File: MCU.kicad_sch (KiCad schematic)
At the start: 51 parts, among them J1 Conn_01x02_Pin, J2 Conn_01x02_Pin, SW1 XRSn_button, U5 F280025PNS, Y2 H130B-16.000-18-3030-EXT-TR

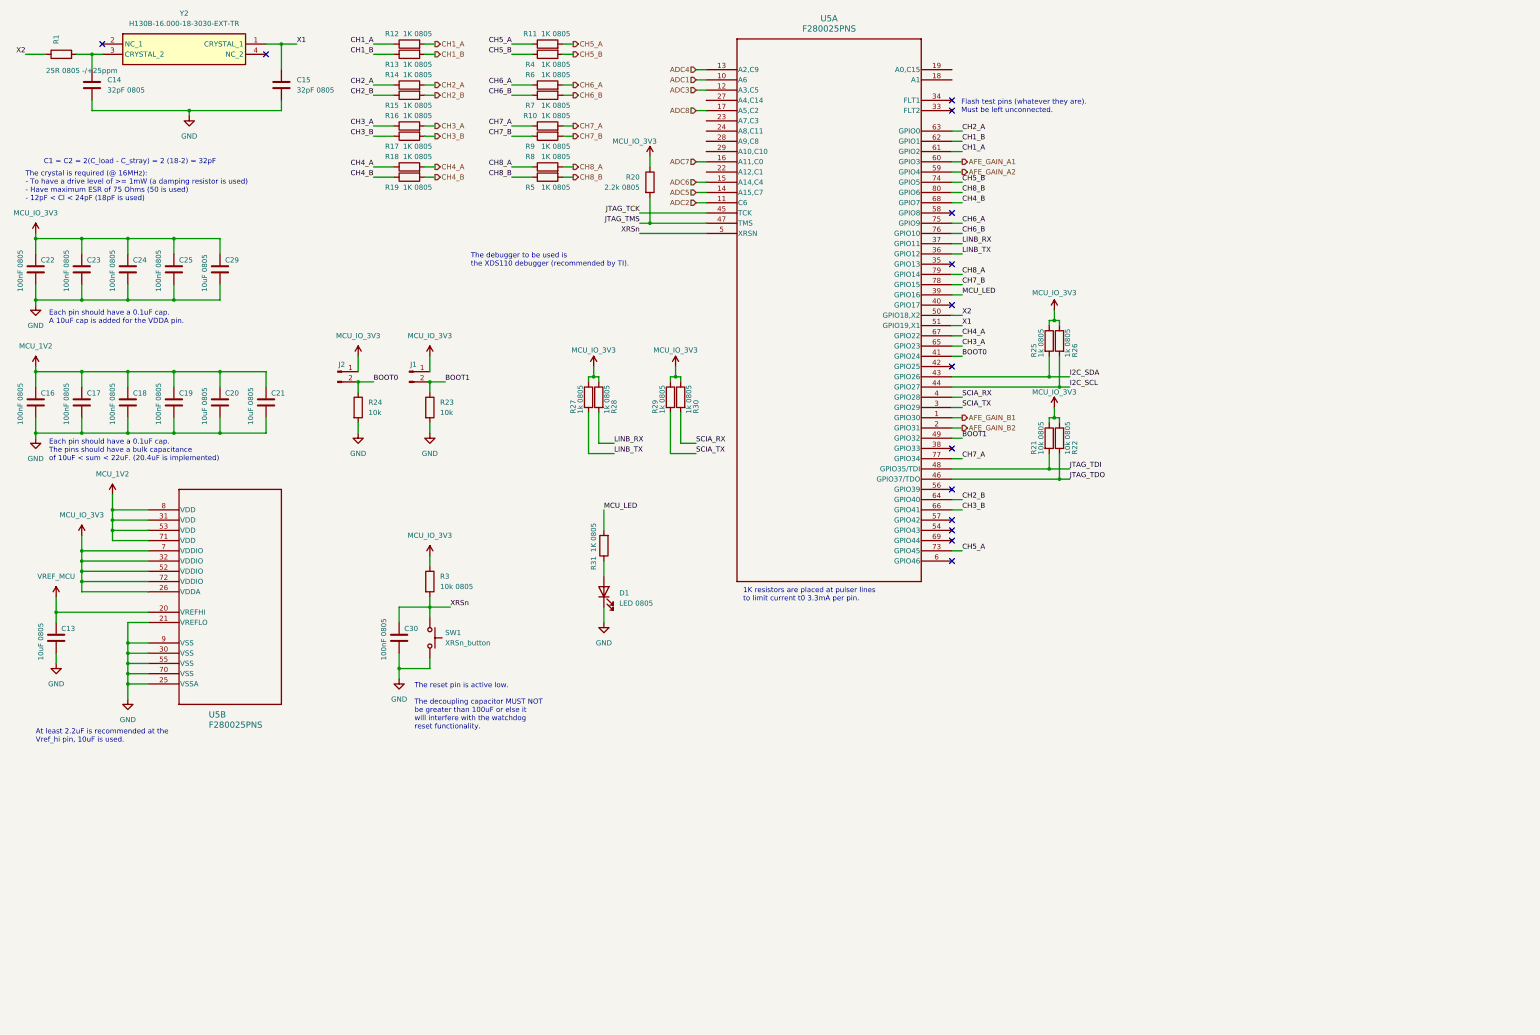
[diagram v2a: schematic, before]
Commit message: finished analog signal chain, added main power components, complete the schematic and form a power budget table
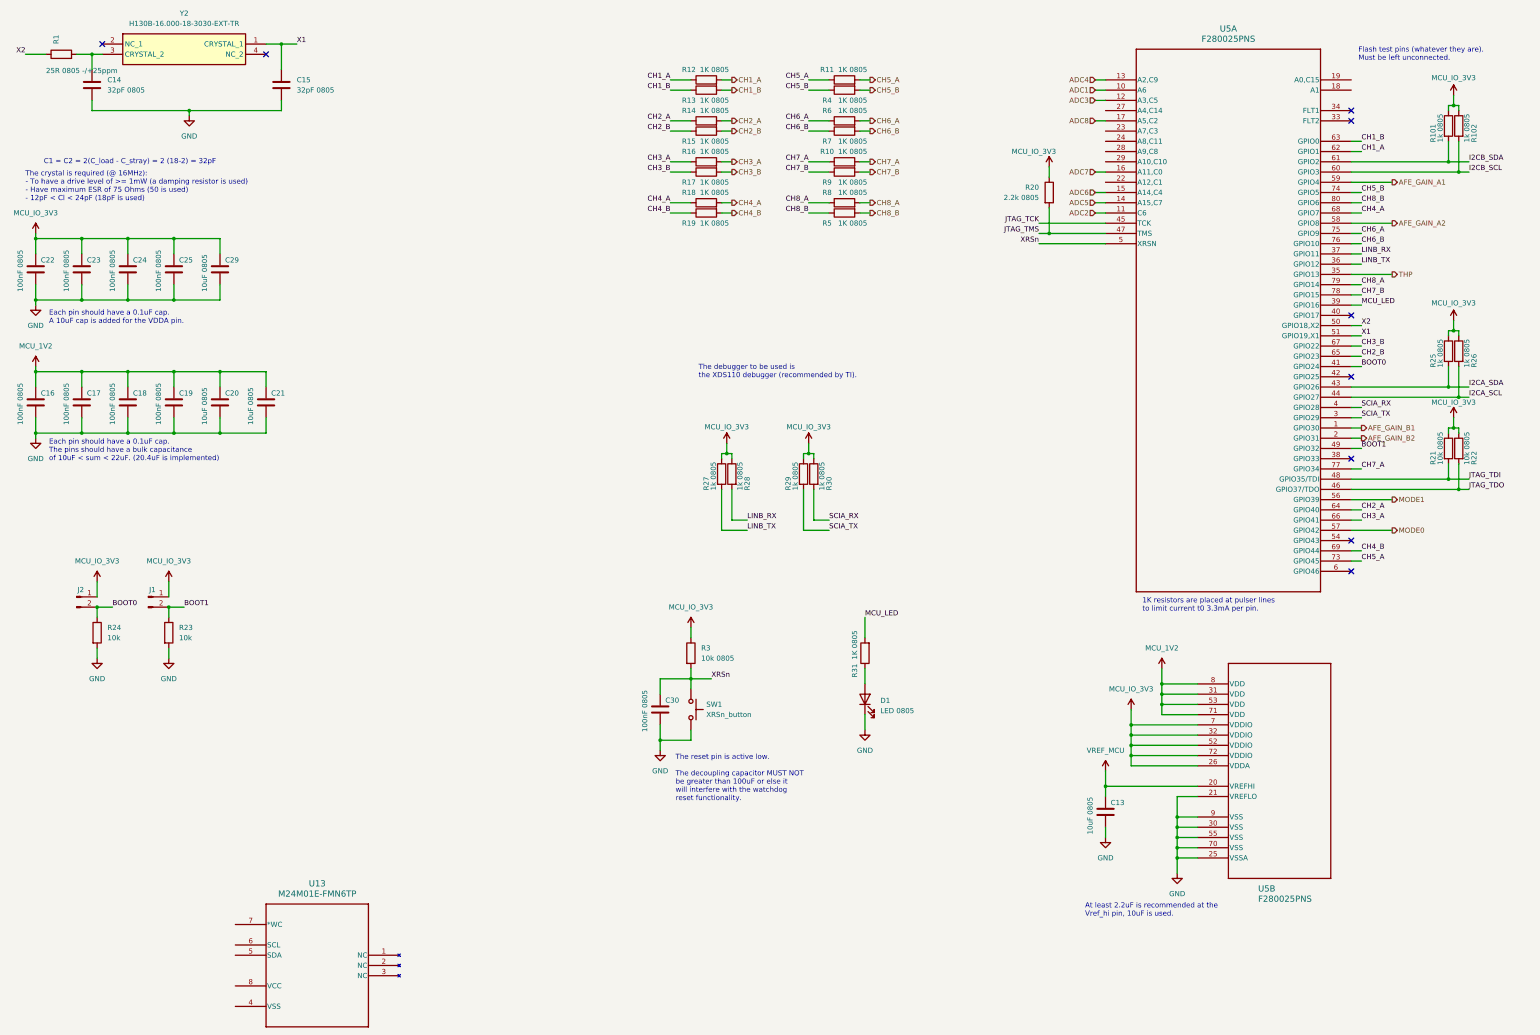
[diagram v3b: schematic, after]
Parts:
- added R101, R102: 1k 0805, symbol Device:R
- added U13: M24M01E-FMN6TP, SO8N_4X5X1P27_STM, symbol M24M01E-FMN6TP:M24M01E-FMN6TP
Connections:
- net AFE_GAIN_A1: now also U5.59 (GPIO4); no longer U5.60 (GPIO3)
- net AFE_GAIN_A2: now also U5.58 (GPIO8); no longer U5.59 (GPIO4)
- net CH1_A: now also U5.62 (GPIO1); no longer U5.61 (GPIO2)
- net CH1_B: now also U5.63 (GPIO0); no longer U5.62 (GPIO1)
- net CH2_A: now also U5.64 (GPIO40); no longer U5.63 (GPIO0)
- net CH2_B: now also U5.65 (GPIO23); no longer U5.64 (GPIO40)
- net CH3_A: now also U5.66 (GPIO41); no longer U5.65 (GPIO23)
- net CH3_B: now also U5.67 (GPIO22); no longer U5.66 (GPIO41)
- net CH4_A: now also U5.68 (GPIO7); no longer U5.67 (GPIO22)
- net CH4_B: now also U5.69 (GPIO44); no longer U5.68 (GPIO7)
- net MCU_IO_3V3: now also R101.1, R102.1
- net THP: now reaches U5.35 (GPIO13)
- net MODE1: now reaches U5.56 (GPIO39)
- net MODE0: now reaches U5.57 (GPIO42)
- net I2C_SCL renamed I2CA_SCL
- net I2C_SDA renamed I2CA_SDA
- new net I2CB_SCL: R102.2, U5.60 (GPIO3)
- new net I2CB_SDA: R101.2, U5.61 (GPIO2)
- no-connect marks 14 -> 9
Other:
- moved on the sheet: C13, C30, D1, J1, J2, R10, R11, R12, R13, R14, R15, R16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

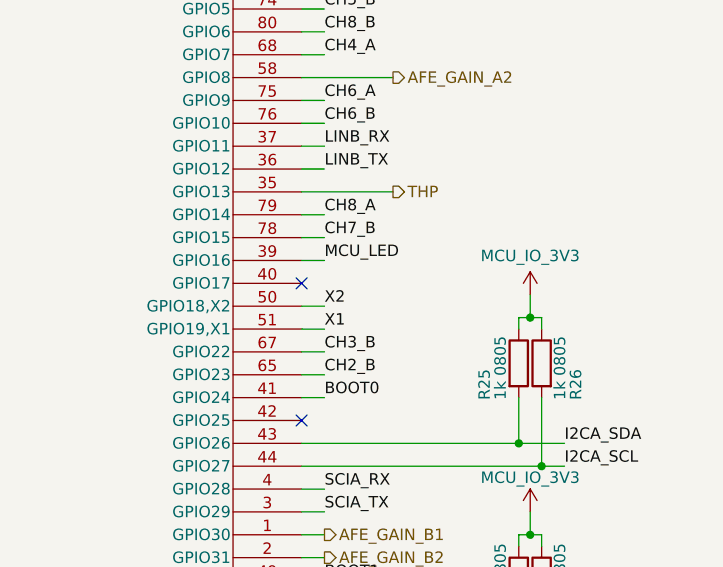
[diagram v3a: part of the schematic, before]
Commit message: finished 50% of power section, 50% remaining + EEPROM & revision
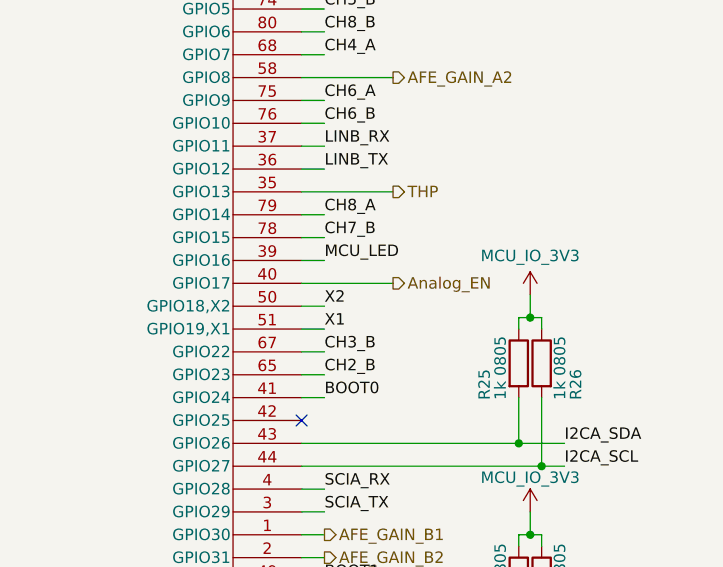
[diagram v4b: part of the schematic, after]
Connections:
- net Analog_EN: now reaches U5.40 (GPIO17)
- no-connect marks 9 -> 8
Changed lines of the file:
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@@
 	)
 	(no_connect
-		(at 345.44 88.9)
-	)
-	(no_connect
 		(at 345.44 104.14)
 	)
@@
 	(wire
 		(pts
+			(xy 345.44 88.9) (xy 355.6 88.9)
+		)
+		(stroke
+			(width 0)
+			(type default)
+		)
+	)
+	(wire
+		(pts
 			(xy 267.97 71.12) (xy 284.48 71.12)
 		)
@@
 		)
 	)
+	(hierarchical_label "Analog_EN"
+		(shape output)
+		(at 355.6 88.9 0)
+		(effects
+			(font
+				(size 1.27 1.27)
+			)
+			(justify left)
+		)
+	)

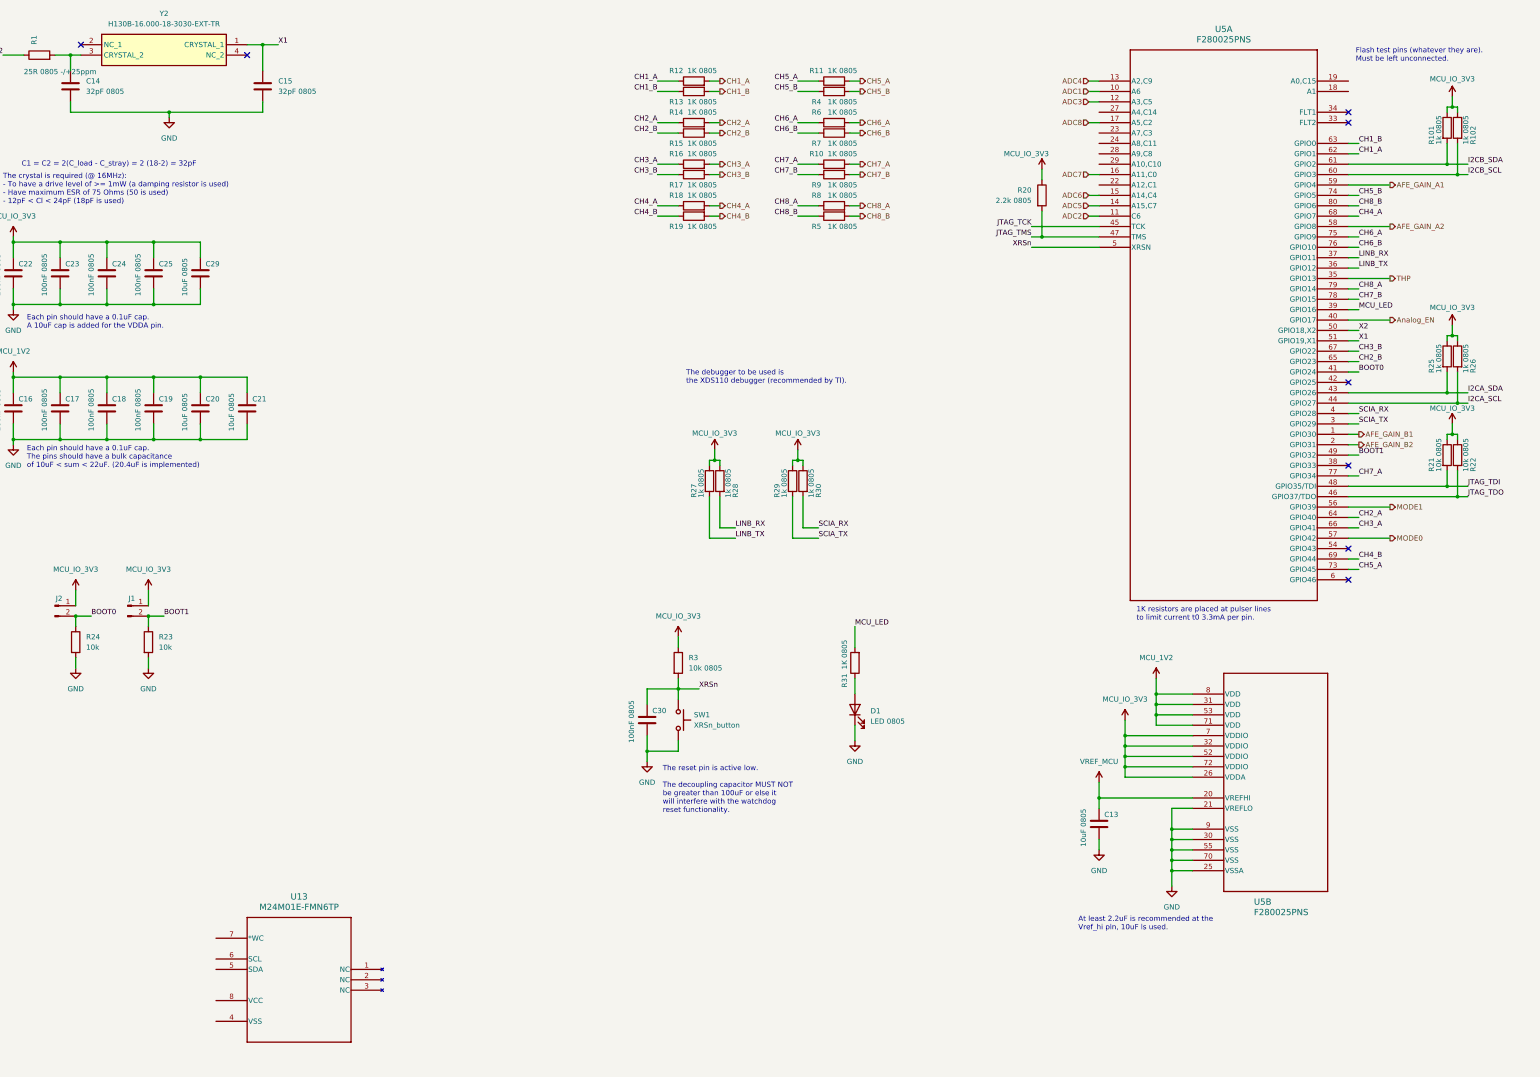
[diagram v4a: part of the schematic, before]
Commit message: 95% done, only headers for communication & power are remaining + RS232 transceiver & 1.5v reference
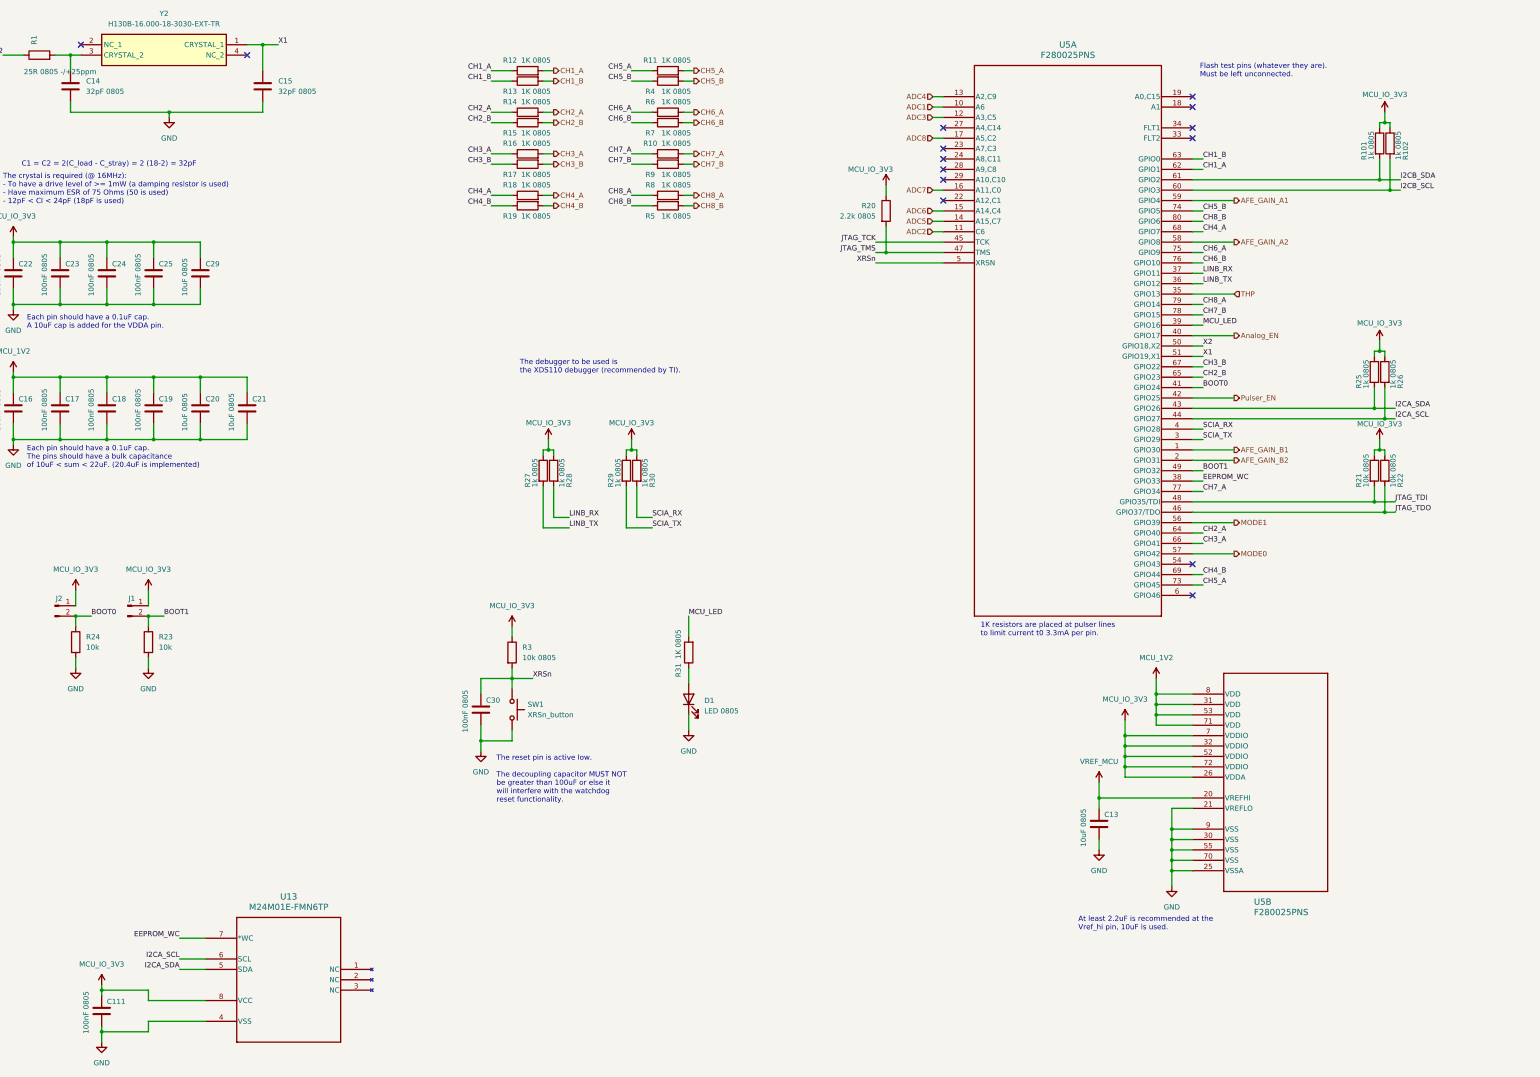
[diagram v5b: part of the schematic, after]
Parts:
- added C111: 100nF 0805, symbol Device:C
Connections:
- net GND: now also U13.4 (VSS), C111.2
- net I2CA_SCL: now also U13.6 (SCL)
- net I2CA_SDA: now also U13.5 (SDA)
- net MCU_IO_3V3: now also U13.8 (VCC), C111.1
- net EEPROM_WC: now reaches U5.38 (GPIO33)
- net EEPROM_WC: now also U13.7 (*WC)
- net Pulser_EN: now reaches U5.42 (GPIO25)
- no-connect marks 8 -> 14
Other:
- moved on the sheet: C30, D1, R10, R101, R102, R11, R12, R13, R14, R15, R16, R17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

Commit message: DONE (inshallah)
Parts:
- added C112, C113, C114, C115, C116, C117: 100nF, symbol Device:C
- added J11: Logger Connector, symbol Connector:Conn_01x03_Pin
- added J12: UART Connector, symbol Connector:Conn_01x03_Pin
- added J13: External UART, digikey-footprints:PinHeader_1x3_P2.5mm_Drill1.1mm, symbol dk_Rectangular-Connectors-Headers-Male-Pins:B3B-XH-A_LF__SN_
- added J14: External I2C, digikey-footprints:PinHeader_1x3_P2.5mm_Drill1.1mm, symbol dk_Rectangular-Connectors-Headers-Male-Pins:B3B-XH-A_LF__SN_
- added J15: JTAG Header, symbol Connector:Conn_01x07_Pin
- added JP19, JP20, JP21: SolderJumper_2_Open, symbol Jumper:SolderJumper_2_Open
- added TP61, TP62, TP63, TP64, TP65, TP66, TP67, TP68, TP69, TP70, TP71, TP72: RCT-0C, digikey-footprints:PROBE_PAD_0805, symbol dk_Test-Points:RCT-0C
- added U17: TRS3221EIPWR, TRS3221EIPWR:SOP65P640X120-16N, symbol TRS3221EIPWR:TRS3221EIPWR
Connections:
- net BOOT0: now also JP19.1 (A)
- net BOOT1: now also JP20.1 (A)
- net CH1_A: now also TP62.1
- net CH1_B: now also TP61.1
- net GND: now also C114.2, C115.2, C116.2, C117.2, J11.3 (Pin_3), J12.3 (Pin_3), J13.1, J14.1, J15.7 (Pin_7), U17.1 (~{EN}), U17.14 (GND)
- net I2CA_SCL: now also TP64.1
- net I2CA_SDA: now also TP63.1
- net I2CB_SCL: now also J14.2, TP68.1
- net I2CB_SDA: now also J14.3, TP67.1
- net JTAG_TCK: now also J15.5 (Pin_5)
- net JTAG_TDI: now also J15.3 (Pin_3), TP65.1
- net JTAG_TDO: now also J15.4 (Pin_4), TP66.1
- net JTAG_TMS: now also J15.6 (Pin_6)
- net LINB_RX: now also J12.1 (Pin_1), TP69.1, U17.9 (ROUT)
- net LINB_TX: now also J12.2 (Pin_2), TP70.1, U17.11 (DIN)
- net MCU_IO_3V3: now also C116.1, C117.1, J15.1 (Pin_1), JP19.2 (B), JP20.2 (B), U17.15 (VCC)
- net SCIA_RX: now also J13.3, TP71.1
- net SCIA_TX: now also J13.2, TP72.1
- net XRSn: now also JP21.2 (B)
- net RS232_FOFF: now reaches U5.54 (GPIO43)
- net RS232_FOFF: now also U17.16 (~{FORCEOFF})
- net RS232_FON: now reaches U5.6 (GPIO46)
- net RS232_FON: now also U17.12 (FORCEON)
- new net: C112.1, U17.2 (C1+)
- new net: C112.2, U17.4 (C1-)
- new net: C115.1, U17.3 (V+)
- new net: C113.1, U17.5 (C2+)
- new net: C113.2, U17.6 (C2-)
- new net: C114.1, U17.7 (V-)
- new net: J15.2 (Pin_2), JP21.1 (A)
- new net RS232_RX: J11.1 (Pin_1), U17.8 (RIN)
- new net RS232_TX: J11.2 (Pin_2), U17.13 (DOUT)
- no-connect marks 14 -> 16
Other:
- note added: "The MCU has no dedicated JTAG reset pin (TRSTn) but theoretically this could work."
- moved on the sheet: C111, C13, C30, D1, J2, R23, R24, R27, R28, R29, R3, R30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

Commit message: started layout, 20-30% done
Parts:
- added J27: Conn_01x02_Pin, Connector_PinHeader_2.54mm:PinHeader_1x02_P2.54mm_Vertical, symbol Connector:Conn_01x02_Pin
- C111, C112, C113, C114, C115, C116, C117, C13, C14, C15, C16, C17, C18, C19, C20, C21, C22, C23, C24, C25, C29, C30: footprint (none) -> Capacitor_SMD:C_0603_1608Metric
- D1: footprint (none) -> LED_SMD:LED_0805_2012Metric
- J1, J2: footprint (none) -> Connector_PinHeader_2.54mm:PinHeader_1x02_P2.54mm_Vertical
- J11, J12: footprint (none) -> Connector_PinHeader_2.54mm:PinHeader_1x03_P2.54mm_Vertical
- J15: footprint (none) -> Connector_PinHeader_2.54mm:PinHeader_1x07_P2.54mm_Vertical
- JP19, JP20, JP21: footprint (none) -> Jumper:SolderJumper-2_P1.3mm_Open_Pad1.0x1.5mm
- R1, R10, R101, R102, R11, R12, R13, R14, R15, R16, R17, R18, R19, R20, R21, R22, R23, R24, R25, R26, R27, R28, R29, R3, R30, R31, R4, R5, R6, R7, R8, R9: footprint (none) -> Resistor_SMD:R_0603_1608Metric
- SW1: footprint (none) -> Button_Switch_SMD:SW_Push_SPST_NO_Alps_SKRK
- U13: footprint SO8N_4X5X1P27_STM -> M24M01E-FMN6TP:SO8N_4X5X1P27_STM
- U5: footprint PQFP_025PNSR_TEX -> F280025PNS:PQFP_025PNSR_TEX
- Y2: footprint H130B16000183030EXTTR -> KiCad:H130B16000183030EXTTR
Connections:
- net CH1_A: now also U5.80 (GPIO6); no longer TP62.1, U5.62 (GPIO1)
- net CH1_B: now also U5.79 (GPIO14); no longer TP61.1, U5.63 (GPIO0)
- net CH2_A: now also U5.78 (GPIO15); no longer U5.64 (GPIO40)
- net CH2_B: now also U5.77 (GPIO34); no longer U5.65 (GPIO23)
- net CH3_A: now also U5.76 (GPIO10); no longer U5.66 (GPIO41)
- net CH3_B: now also U5.75 (GPIO9); no longer U5.67 (GPIO22)
- net CH4_A: now also U5.74 (GPIO5); no longer U5.68 (GPIO7)
- net CH4_B: now also U5.73 (GPIO45); no longer U5.69 (GPIO44)
- net CH5_A: now also TP62.1, U5.62 (GPIO1); no longer U5.73 (GPIO45)
- net CH5_B: now also TP61.1, U5.63 (GPIO0); no longer U5.74 (GPIO5)
- net CH6_A: now also U5.64 (GPIO40); no longer U5.75 (GPIO9)
- net CH6_B: now also U5.65 (GPIO23); no longer U5.76 (GPIO10)
- net CH7_A: now also U5.66 (GPIO41); no longer U5.77 (GPIO34)
- net CH7_B: now also U5.67 (GPIO22); no longer U5.78 (GPIO15)
- net CH8_A: now also U5.68 (GPIO7); no longer U5.79 (GPIO14)
- net CH8_B: now also U5.69 (GPIO44); no longer U5.80 (GPIO6)
- net I2CB_SCL: now also J27.2 (Pin_2)
- net I2CB_SDA: now also J27.1 (Pin_1)
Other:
- moved on the sheet: C117, J15, JP21
